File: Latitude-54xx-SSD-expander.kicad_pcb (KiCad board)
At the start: 4 copper layers, 60 x 112 mm, 29 parts, among them J1 Bus_M.2_Socket_M, J2 M-key-full, J3 M-key-full, J4 qwiic, J5 refqwock, J6 refqwock, U2 clockbuffer_RENESAS_9DBL411BG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

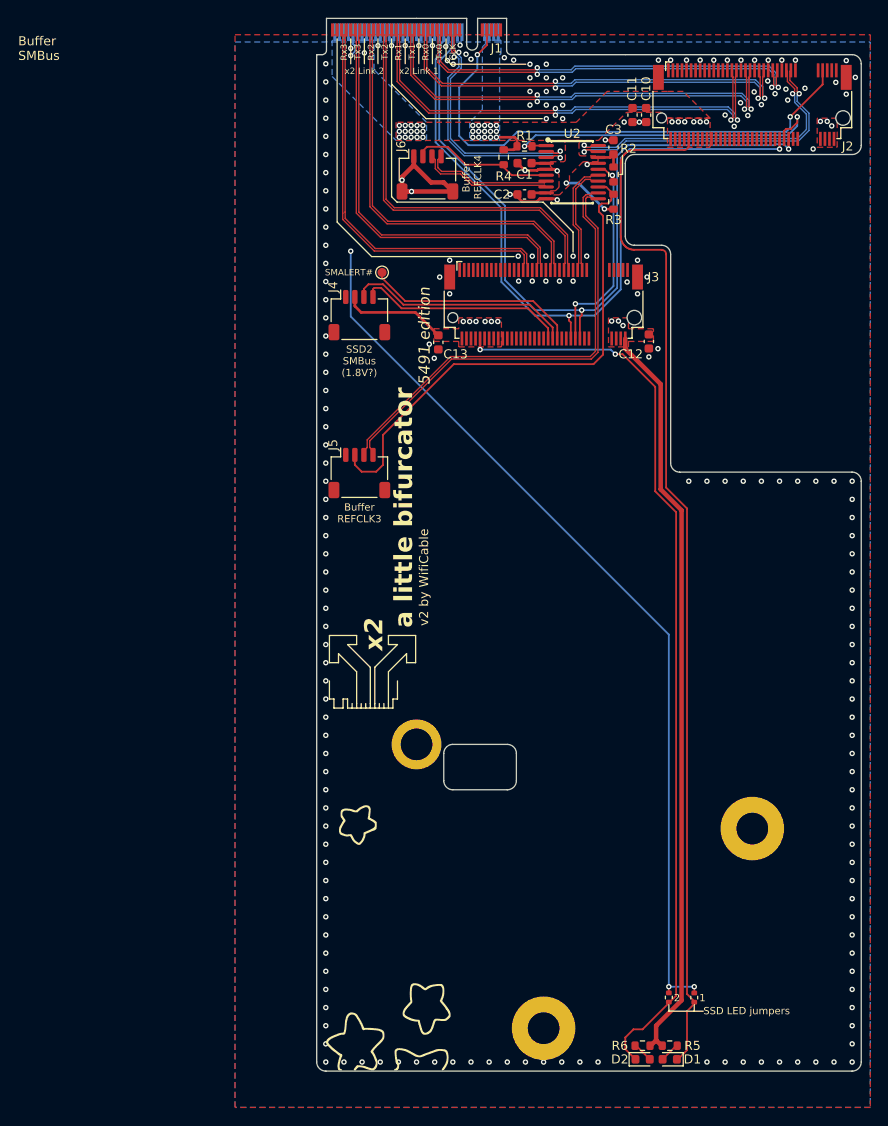
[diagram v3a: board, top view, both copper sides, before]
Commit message: fixed m.2 standoff footprints, v2 done?
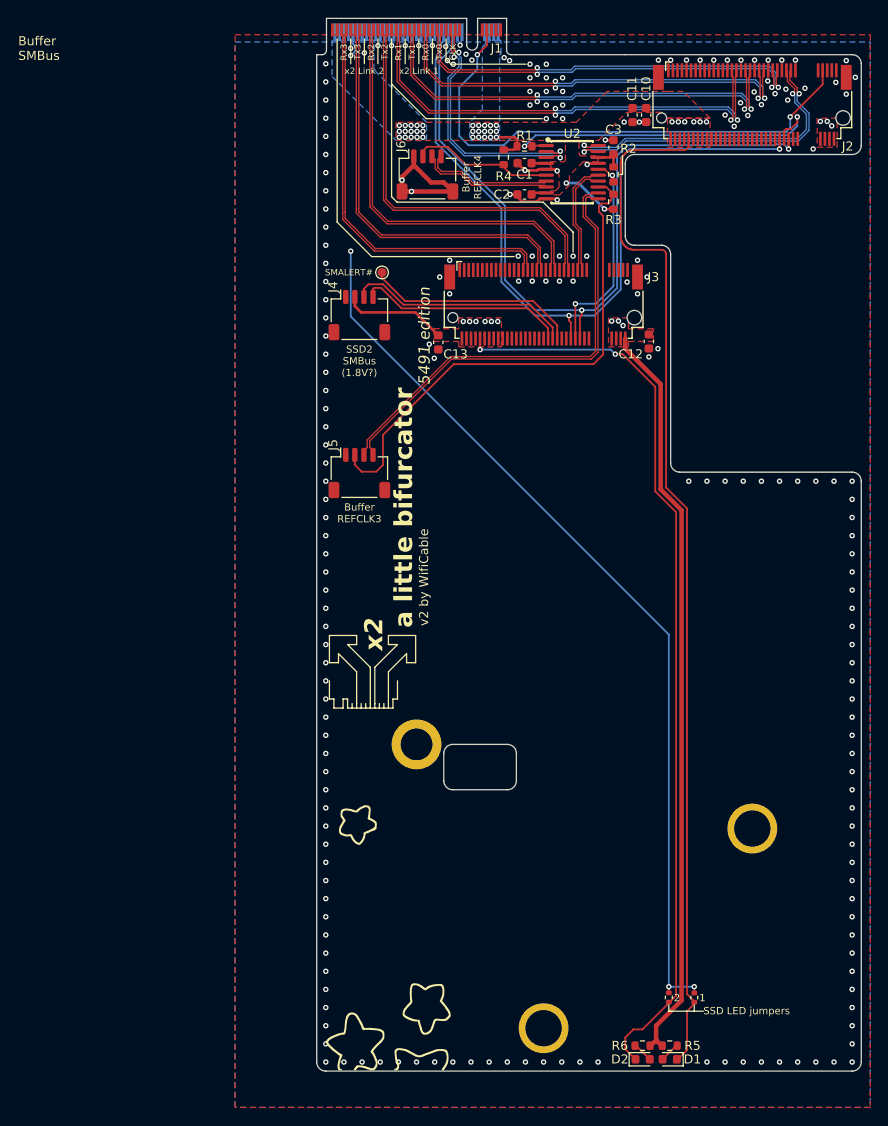
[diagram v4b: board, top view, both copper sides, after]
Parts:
- H2, H3: footprint MountingHole:MountingHole_3.5mm_Pad -> MountingHole:MountingHole_4mm_Pad
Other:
- board text added: "v2 TODO: [x] fix impedance (and for jlc now) [x] change clock buffer [x] use proper m.2 standoffs [x] add host activity led option [x] remove ground around diffpairs"
- board text removed: "v2 TODO: [x] fix impedance (and for jlc now) [x] change clock buffer [ ] use proper m.2 standoffs [x] add host activity led option [x] remove ground around diffpairs"
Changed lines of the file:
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@@
 		)
 	)
-	(footprint "MountingHole:MountingHole_3.5mm_Pad"
+	(footprint "MountingHole:MountingHole_4mm_Pad"
 		(layer "F.Cu")
 		(at 104.000001 151.275)
-		(descr "Mounting Hole 3.5mm")
-		(tags "mounting hole 3.5mm")
+		(descr "Mounting Hole 4mm, generated by kicad-footprint-generator mountinghole.py")
+		(tags "mountinghole")
 		(property "Reference" "H3"
-			(at 0 -4.5 0)
+			(at 0 -4.95 0)
 			(layer "F.SilkS")
 			(hide yes)
@@
 		)
 		(property "Value" "MountingHole_Pad"
-			(at 0 4.5 0)
+			(at 0 4.95 0)
 			(layer "F.Fab")
 			(effects
@@
 		(property "Datasheet" "~"
 			(at 0 0 0)
-			(unlocked yes)
 			(layer "F.Fab")
 			(hide yes)
@@
 		(property "Description" "Mounting Hole with connection"
 			(at 0 0 0)
-			(unlocked yes)
 			(layer "F.Fab")
 			(hide yes)
@@
 		(fp_circle
 			(center 0 0)
-			(end 3.5 0.000001)
+			(end 2.75 0)
 			(stroke
 				(width 0.15)
@@
 		(fp_circle
 			(center 0 0)
-			(end 3.75 0)
+			(end 3 0)
 			(stroke
 				(width 0.05)
@@
 		(pad "1" thru_hole circle
 			(at 0 0)
-			(size 7 7)
-			(drill 3.5)
+			(size 5.5 5.5)
+			(drill 4)
 			(layers "*.Cu" "*.Mask")
 			(remove_unused_layers no)
@@
 			(pinfunction "1")
 			(pintype "input")
+			(zone_connect 2)
 		)
 		(embedded_fonts no)
+		(model "C:/Users/WifiCable/Documents/KiCad/easyeda2kicad/m2-standoff.3dshapes/SMD_BD5.6-D4.1.step"
+			(offset
+				(xyz 0 0 0)
+			)
+			(scale
+				(xyz 1 1 1)
+			)
+			(rotate
+				(xyz 0 0 0)
+			)
+		)
 	)
 	(footprint "Connector_JST:JST_SH_SM04B-SRSS-TB_1x04-1MP_P1.00mm_Horizontal"
@@
 		)
 	)
-	(footprint "MountingHole:MountingHole_3.5mm_Pad"
+	(footprint "MountingHole:MountingHole_4mm_Pad"
 		(layer "F.Cu")
 		(at 127 129.275)
-		(descr "Mounting Hole 3.5mm")
-		(tags "mounting hole 3.5mm")
+		(descr "Mounting Hole 4mm, generated by kicad-footprint-generator mountinghole.py")
+		(tags "mountinghole")
 		(property "Reference" "H2"
-			(at 0 -4.5 0)
+			(at 0 -4.95 0)
 			(layer "F.SilkS")
 			(hide yes)
@@
 		)
 		(property "Value" "MountingHole_Pad"
-			(at 0 4.5 0)
+			(at 0 4.95 0)
 			(layer "F.Fab")
 			(effects
@@
 		(property "Datasheet" "~"
 			(at 0 0 0)
-			(unlocked yes)
 			(layer "F.Fab")
 			(hide yes)
@@
 		(property "Description" "Mounting Hole with connection"
 			(at 0 0 0)
-			(unlocked yes)
 			(layer "F.Fab")
 			(hide yes)
@@
 		(fp_circle
 			(center 0 0)
-			(end 3.5 0)
+			(end 2.75 0)
 			(stroke
 				(width 0.15)
@@
 		(fp_circle
 			(center 0 0)
-			(end 3.75 0)
+			(end 3 0)
 			(stroke
 				(width 0.05)
@@
 		(pad "1" thru_hole circle
 			(at 0 0)
-			(size 7 7)
-			(drill 3.5)
+			(size 5.5 5.5)
+			(drill 4)
 			(layers "*.Cu" "*.Mask")
 			(remove_unused_layers no)
@@
 			(pinfunction "1")
 			(pintype "input")
+			(zone_connect 2)
 		)
 		(embedded_fonts no)
+		(model "C:/Users/WifiCable/Documents/KiCad/easyeda2kicad/m2-standoff.3dshapes/SMD_BD5.6-D4.1.step"
+			(offset
+				(xyz 0 0 0)
+			)
+			(scale
+				(xyz 1 1 1)
+			)
+			(rotate
+				(xyz 0 0 0)
+			)
+		)
 	)
 	(footprint "Resistor_SMD:R_0603_1608Metric"
@@
 		)
 	)
-	(gr_text "v2 TODO:\n[x] fix impedance (and for jlc now)\n[x] change clock buffer\n[ ] use proper m.2 standoffs\n[x] add host activity led option\n[x] remove ground around diffpairs"
+	(gr_text "v2 TODO:\n[x] fix impedance (and for jlc now)\n[x] change clock buffer\n[x] use proper m.2 standoffs\n[x] add host activity led option\n[x] remove ground around diffpairs"
 		(at 146 62 0)
 		(layer "User.1")
@@
 	)
 	(via
-		(at 99.675 44.325)
+		(at 99.65 44.325)
 		(size 0.6)
 		(drill 0.3)
@@
 	)
 	(via
-		(at 100.7 44.6)
+		(at 100.25 44.65)
 		(size 0.6)
 		(drill 0.3)
@@
 	)
 	(via
-		(at 96 44.5)
+		(at 96.1 44.6)
 		(size 0.6)
 		(drill 0.3)
@@
 				(xy 81.1 43.8) (xy 81.8 43.1) (xy 81.8 43.3) (xy 82.4 43.3) (xy 82.4 43.6) (xy 83.1 43.6) (xy 83.1 43.3)
 				(xy 83.9 43.3) (xy 83.9 44.1) (xy 84.6 44.1) (xy 84.6 43.3) (xy 92.9 43.3) (xy 92.9 43.386) (xy 93.6 43.4)
-				(xy 93.6 43.3) (xy 95.5 43.3) (xy 97.2 45) (xy 100.9 45) (xy 101.6 44.3) (xy 116.15 44.3) (xy 116.15 46.5)
-				(xy 134.5 46.5) (xy 134.5 47.3) (xy 131.35 50.45) (xy 131.35 52.3) (xy 122.5 52.35) (xy 122.5 50.9)
-				(xy 119.45 47.85) (xy 116.15 47.85) (xy 110.9 47.85) (xy 107.45 51.3) (xy 87.6 51.3) (xy 87.6 53.6)
-				(xy 104.6 53.6) (xy 104.6 56.4) (xy 105.55 56.4) (xy 105.95 56.8) (xy 105.65 57.1) (xy 105.65 58.05)
-				(xy 104.6 58.75) (xy 104.6 59.7) (xy 105.65 59.7) (xy 106.95 58.4) (xy 106.95 57.3) (xy 108.5 55.75)
-				(xy 110.9 55.75) (xy 110.9 52.8) (xy 111.2 52.5) (xy 111.2 53.8) (xy 112.2 53.8) (xy 112.4 54) (xy 112.4 55.5)
-				(xy 112.4 65.5) (xy 112.1 65.8) (xy 112.1 66.8) (xy 110.9 66.8) (xy 110.9 65.9) (xy 100.85 65.9)
-				(xy 100.85 66.4) (xy 98.9 66.4) (xy 85 66.4) (xy 81.1 62.5)
+				(xy 93.6 43.3) (xy 95.5 43.3) (xy 96.5 44.3) (xy 95.8 44.3) (xy 95.8 45) (xy 100.5 45) (xy 101.2 44.3)
+				(xy 116.15 44.3) (xy 116.15 46.5) (xy 134.5 46.5) (xy 134.5 47.3) (xy 131.35 50.45) (xy 131.35 52.3)
+				(xy 122.5 52.35) (xy 122.5 50.9) (xy 119.45 47.85) (xy 116.15 47.85) (xy 110.9 47.85) (xy 107.45 51.3)
+				(xy 87.6 51.3) (xy 87.6 53.6) (xy 104.6 53.6) (xy 104.6 56.4) (xy 105.55 56.4) (xy 105.95 56.8)
+				(xy 105.65 57.1) (xy 105.65 58.05) (xy 104.6 58.75) (xy 104.6 59.7) (xy 105.65 59.7) (xy 106.95 58.4)
+				(xy 106.95 57.3) (xy 108.5 55.75) (xy 110.9 55.75) (xy 110.9 52.8) (xy 111.2 52.5) (xy 111.2 53.8)
+				(xy 112.2 53.8) (xy 112.4 54) (xy 112.4 55.5) (xy 112.4 65.5) (xy 112.1 65.8) (xy 112.1 66.8) (xy 110.9 66.8)
+				(xy 110.9 65.9) (xy 100.85 65.9) (xy 100.85 66.4) (xy 98.9 66.4) (xy 85 66.4) (xy 81.1 62.5)
 			)
 		)
@@
 		(polygon
 			(pts
-				(xy 100.4 44.3) (xy 99.4 43.7) (xy 99.4 52.3) (xy 114.1 52.3) (xy 114.1 54.7) (xy 139.2 54.7) (xy 139.2 44.3)
+				(xy 100.4 44.3) (xy 99.8 43.7) (xy 99.8 42.65) (xy 99.35 42.65) (xy 99.35 43.95) (xy 99.2 44.1)
+				(xy 99.2 52.3) (xy 114.1 52.3) (xy 114.1 54.7) (xy 139.2 54.7) (xy 139.2 44.3)
 			)
 		)
